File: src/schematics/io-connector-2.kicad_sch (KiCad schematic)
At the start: 1 part

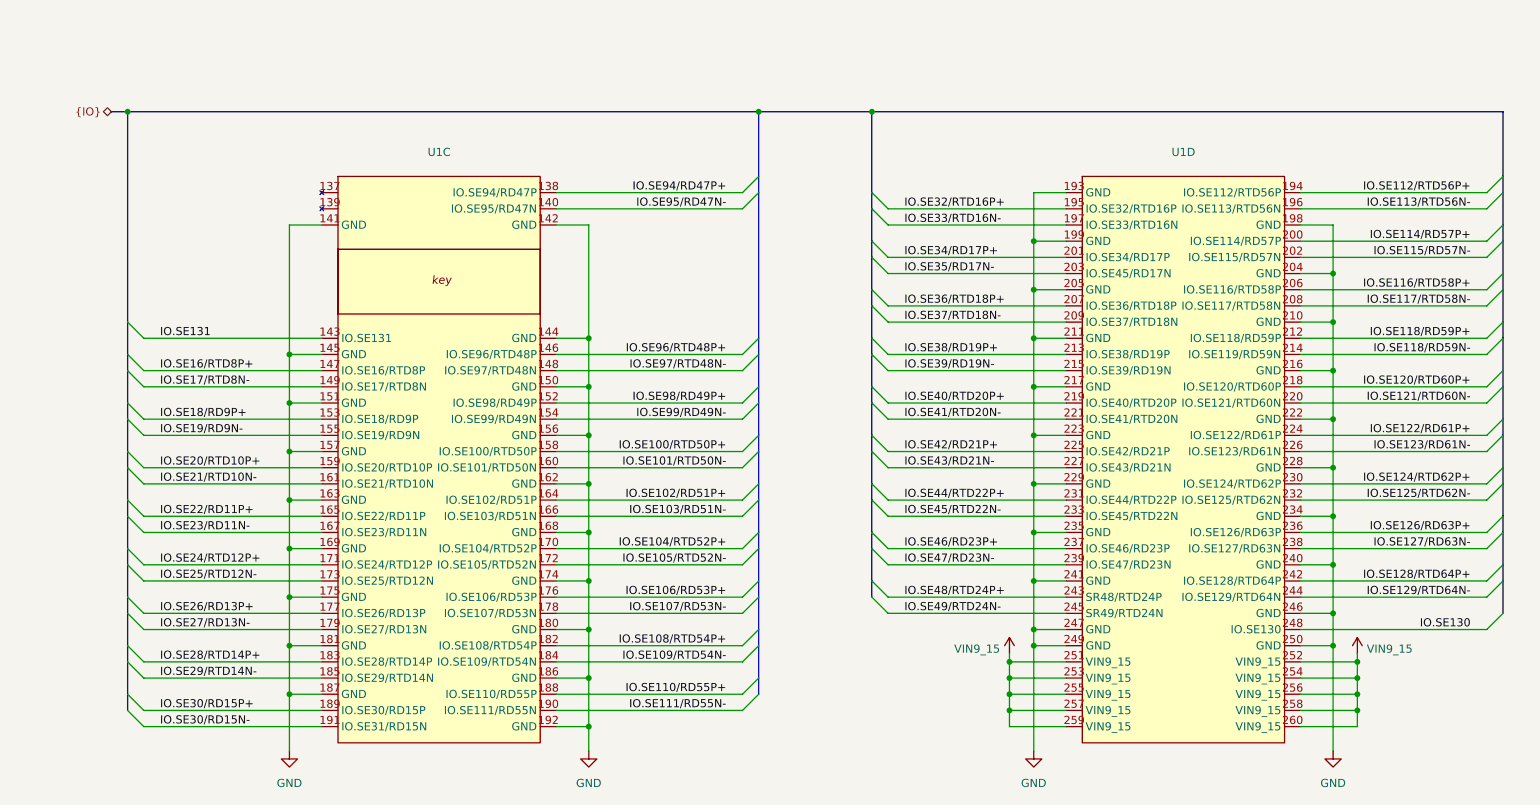
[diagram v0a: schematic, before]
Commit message: Adds draft of IO connector schematic connections to FPGA
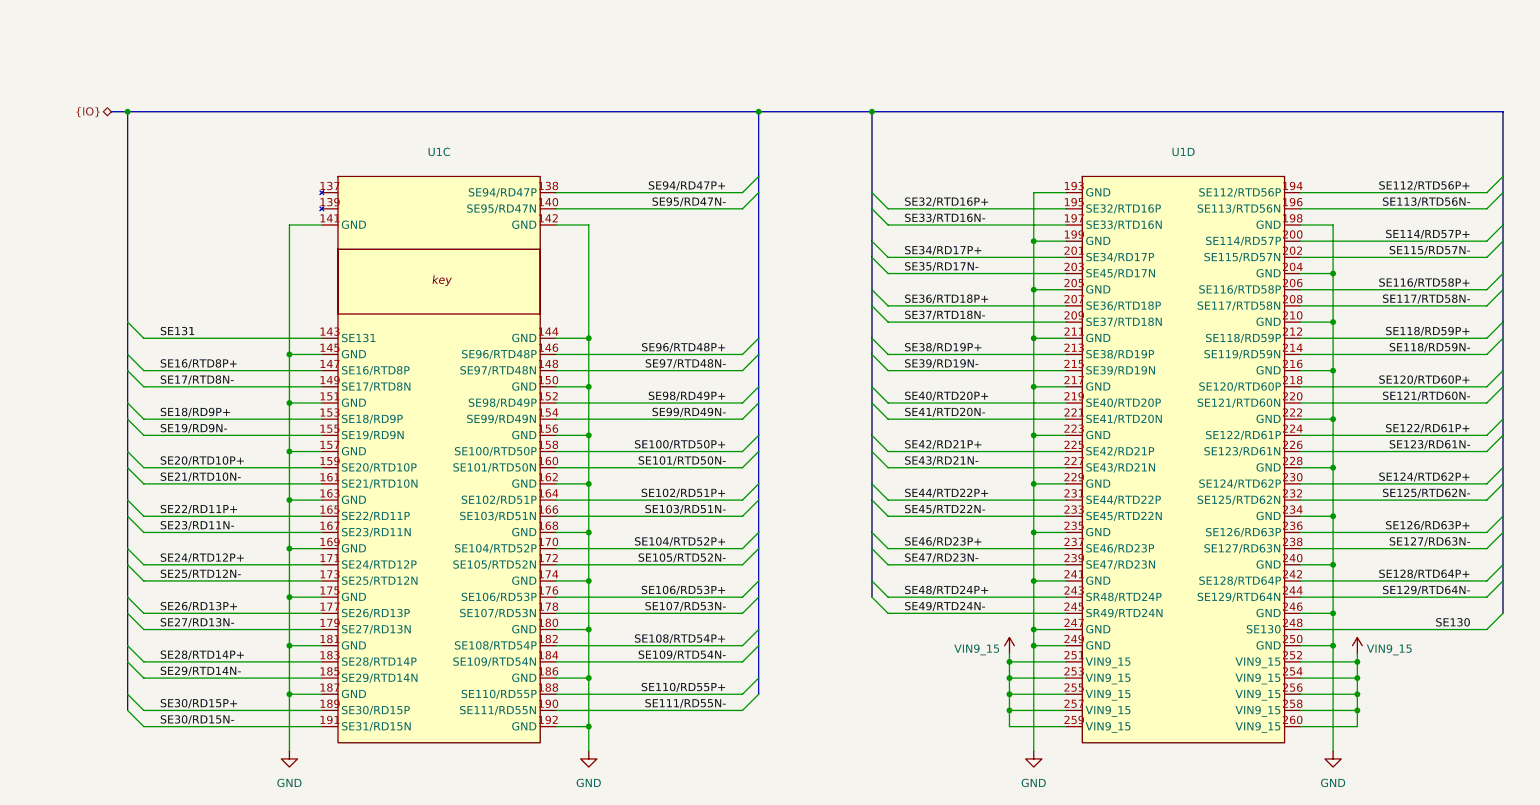
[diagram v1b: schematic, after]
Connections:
- net IO.SE100/RTD50P+ renamed SE100/RTD50P+
- net IO.SE101/RTD50N- renamed SE101/RTD50N-
- net IO.SE102/RD51P+ renamed SE102/RD51P+
- net IO.SE103/RD51N- renamed SE103/RD51N-
- net IO.SE104/RTD52P+ renamed SE104/RTD52P+
- net IO.SE105/RTD52N- renamed SE105/RTD52N-
- net IO.SE106/RD53P+ renamed SE106/RD53P+
- net IO.SE107/RD53N- renamed SE107/RD53N-
- net IO.SE108/RTD54P+ renamed SE108/RTD54P+
- net IO.SE109/RTD54N- renamed SE109/RTD54N-
- net IO.SE110/RD55P+ renamed SE110/RD55P+
- net IO.SE111/RD55N- renamed SE111/RD55N-
- net IO.SE112/RTD56P+ renamed SE112/RTD56P+
- net IO.SE113/RTD56N- renamed SE113/RTD56N-
- net IO.SE114/RD57P+ renamed SE114/RD57P+
- net IO.SE115/RD57N- renamed SE115/RD57N-
- net IO.SE116/RTD58P+ renamed SE116/RTD58P+
- net IO.SE117/RTD58N- renamed SE117/RTD58N-
- net IO.SE118/RD59N- renamed SE118/RD59N-
- net IO.SE118/RD59P+ renamed SE118/RD59P+
- net IO.SE120/RTD60P+ renamed SE120/RTD60P+
- net IO.SE121/RTD60N- renamed SE121/RTD60N-
- net IO.SE122/RD61P+ renamed SE122/RD61P+
- net IO.SE123/RD61N- renamed SE123/RD61N-
- net IO.SE124/RTD62P+ renamed SE124/RTD62P+
- net IO.SE125/RTD62N- renamed SE125/RTD62N-
- net IO.SE126/RD63P+ renamed SE126/RD63P+
- net IO.SE127/RD63N- renamed SE127/RD63N-
- net IO.SE128/RTD64P+ renamed SE128/RTD64P+
- net IO.SE129/RTD64N- renamed SE129/RTD64N-
- net IO.SE130 renamed SE130
- net IO.SE131 renamed SE131
- net IO.SE16/RTD8P+ renamed SE16/RTD8P+
- net IO.SE17/RTD8N- renamed SE17/RTD8N-
- net IO.SE18/RD9P+ renamed SE18/RD9P+
- net IO.SE19/RD9N- renamed SE19/RD9N-
- net IO.SE20/RTD10P+ renamed SE20/RTD10P+
- net IO.SE21/RTD10N- renamed SE21/RTD10N-
- net IO.SE22/RD11P+ renamed SE22/RD11P+
- net IO.SE23/RD11N- renamed SE23/RD11N-
- net IO.SE24/RTD12P+ renamed SE24/RTD12P+
- net IO.SE25/RTD12N- renamed SE25/RTD12N-
- net IO.SE26/RD13P+ renamed SE26/RD13P+
- net IO.SE27/RD13N- renamed SE27/RD13N-
- net IO.SE28/RTD14P+ renamed SE28/RTD14P+
- net IO.SE29/RTD14N- renamed SE29/RTD14N-
- net IO.SE30/RD15N- renamed SE30/RD15N-
- net IO.SE30/RD15P+ renamed SE30/RD15P+
- net IO.SE32/RTD16P+ renamed SE32/RTD16P+
- net IO.SE33/RTD16N- renamed SE33/RTD16N-
- net IO.SE34/RD17P+ renamed SE34/RD17P+
- net IO.SE35/RD17N- renamed SE35/RD17N-
- net IO.SE36/RTD18P+ renamed SE36/RTD18P+
- net IO.SE37/RTD18N- renamed SE37/RTD18N-
- net IO.SE38/RD19P+ renamed SE38/RD19P+
- net IO.SE39/RD19N- renamed SE39/RD19N-
- net IO.SE40/RTD20P+ renamed SE40/RTD20P+
- net IO.SE41/RTD20N- renamed SE41/RTD20N-
- net IO.SE42/RD21P+ renamed SE42/RD21P+
- net IO.SE43/RD21N- renamed SE43/RD21N-
- net IO.SE44/RTD22P+ renamed SE44/RTD22P+
- net IO.SE45/RTD22N- renamed SE45/RTD22N-
- net IO.SE46/RD23P+ renamed SE46/RD23P+
- net IO.SE47/RD23N- renamed SE47/RD23N-
- net IO.SE48/RTD24P+ renamed SE48/RTD24P+
- net IO.SE49/RTD24N- renamed SE49/RTD24N-
- net IO.SE94/RD47P+ renamed SE94/RD47P+
- net IO.SE95/RD47N- renamed SE95/RD47N-
- net IO.SE96/RTD48P+ renamed SE96/RTD48P+
- net IO.SE97/RTD48N- renamed SE97/RTD48N-
- net IO.SE98/RD49P+ renamed SE98/RD49P+
- net IO.SE99/RD49N- renamed SE99/RD49N-

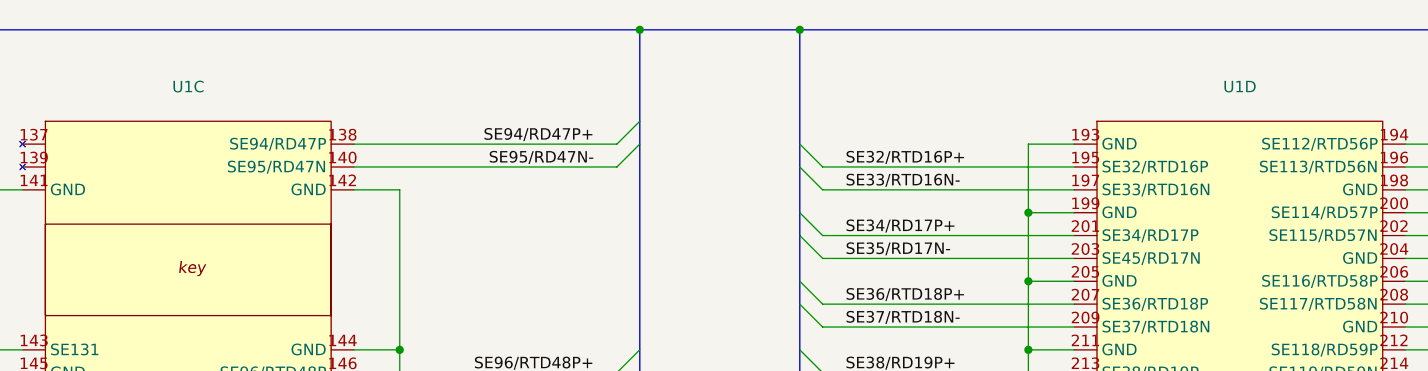
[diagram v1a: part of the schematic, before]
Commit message: Adds the clock oscillator
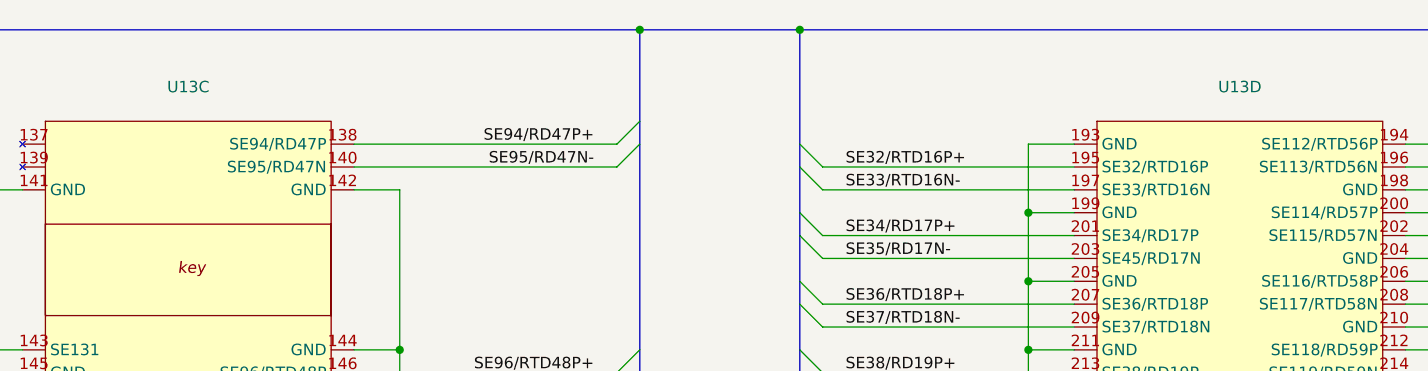
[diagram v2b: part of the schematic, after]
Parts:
- renumbered U1 to U13
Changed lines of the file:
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@@
 		(dnp no)
 		(fields_autoplaced yes)
-		(property "Reference" "U1"
+		(property "Reference" "U13"
 			(at 208.915 44.45 0)
 			(effects
@@
 			(project "ecap5-bsom"
 				(path "/c5fd18a3-9aa0-4151-b6e0-94da3d606686/25311f3d-42bc-4bc6-b069-9a914cc16127/b8034c88-bc29-48fe-94a3-92f685be2030"
-					(reference "U1")
+					(reference "U13")
 					(unit 4)
 				)
@@
 		(dnp no)
 		(fields_autoplaced yes)
-		(property "Reference" "#PWR033"
+		(property "Reference" "#PWR0149"
 			(at 115.57 144.78 0)
 			(effects
@@
 			(project "ecap5-bsom"
 				(path "/c5fd18a3-9aa0-4151-b6e0-94da3d606686/25311f3d-42bc-4bc6-b069-9a914cc16127/b8034c88-bc29-48fe-94a3-92f685be2030"
-					(reference "#PWR033")
+					(reference "#PWR0149")
 					(unit 1)
 				)
@@
 		(on_board yes)
 		(dnp no)
-		(property "Reference" "#PWR034"
+		(property "Reference" "#PWR0146"
 			(at 181.61 127 0)
 			(effects
@@
 			(project "ecap5-bsom"
 				(path "/c5fd18a3-9aa0-4151-b6e0-94da3d606686/25311f3d-42bc-4bc6-b069-9a914cc16127/b8034c88-bc29-48fe-94a3-92f685be2030"
-					(reference "#PWR034")
+					(reference "#PWR0146")
 					(unit 1)
 				)
@@
 	)
 	(symbol
-		(lib_name "IO_CONN_1")
 		(lib_id "ECAP5-BSOM:IO_CONN")
 		(at 92.71 92.71 0)
@@
 		(dnp no)
 		(fields_autoplaced yes)
-		(property "Reference" "U1"
+		(property "Reference" "U13"
 			(at 92.075 44.45 0)
 			(effects
@@
 			(project "ecap5-bsom"
 				(path "/c5fd18a3-9aa0-4151-b6e0-94da3d606686/25311f3d-42bc-4bc6-b069-9a914cc16127/b8034c88-bc29-48fe-94a3-92f685be2030"
-					(reference "U1")
+					(reference "U13")
 					(unit 3)
 				)
@@
 		(dnp no)
 		(fields_autoplaced yes)
-		(property "Reference" "#PWR036"
+		(property "Reference" "#PWR0151"
 			(at 232.41 144.78 0)
 			(effects
@@
 			(project "ecap5-bsom"
 				(path "/c5fd18a3-9aa0-4151-b6e0-94da3d606686/25311f3d-42bc-4bc6-b069-9a914cc16127/b8034c88-bc29-48fe-94a3-92f685be2030"
-					(reference "#PWR036")
+					(reference "#PWR0151")
 					(unit 1)
 				)
@@
 		(dnp no)
 		(fields_autoplaced yes)
-		(property "Reference" "#PWR030"
+		(property "Reference" "#PWR0148"
 			(at 68.58 144.78 0)
 			(effects
@@
 			(project "ecap5-bsom"
 				(path "/c5fd18a3-9aa0-4151-b6e0-94da3d606686/25311f3d-42bc-4bc6-b069-9a914cc16127/b8034c88-bc29-48fe-94a3-92f685be2030"
-					(reference "#PWR030")
+					(reference "#PWR0148")
 					(unit 1)
 				)
@@
 		(on_board yes)
 		(dnp no)
-		(property "Reference" "#PWR039"
+		(property "Reference" "#PWR0147"
 			(at 236.22 127 0)
 			(effects
@@
 			(project "ecap5-bsom"
 				(path "/c5fd18a3-9aa0-4151-b6e0-94da3d606686/25311f3d-42bc-4bc6-b069-9a914cc16127/b8034c88-bc29-48fe-94a3-92f685be2030"
-					(reference "#PWR039")
+					(reference "#PWR0147")
 					(unit 1)
 				)
@@
 		(dnp no)
 		(fields_autoplaced yes)
-		(property "Reference" "#PWR035"
+		(property "Reference" "#PWR0150"
 			(at 185.42 144.78 0)
 			(effects
@@
 			(project "ecap5-bsom"
 				(path "/c5fd18a3-9aa0-4151-b6e0-94da3d606686/25311f3d-42bc-4bc6-b069-9a914cc16127/b8034c88-bc29-48fe-94a3-92f685be2030"
-					(reference "#PWR035")
+					(reference "#PWR0150")
 					(unit 1)
 				)

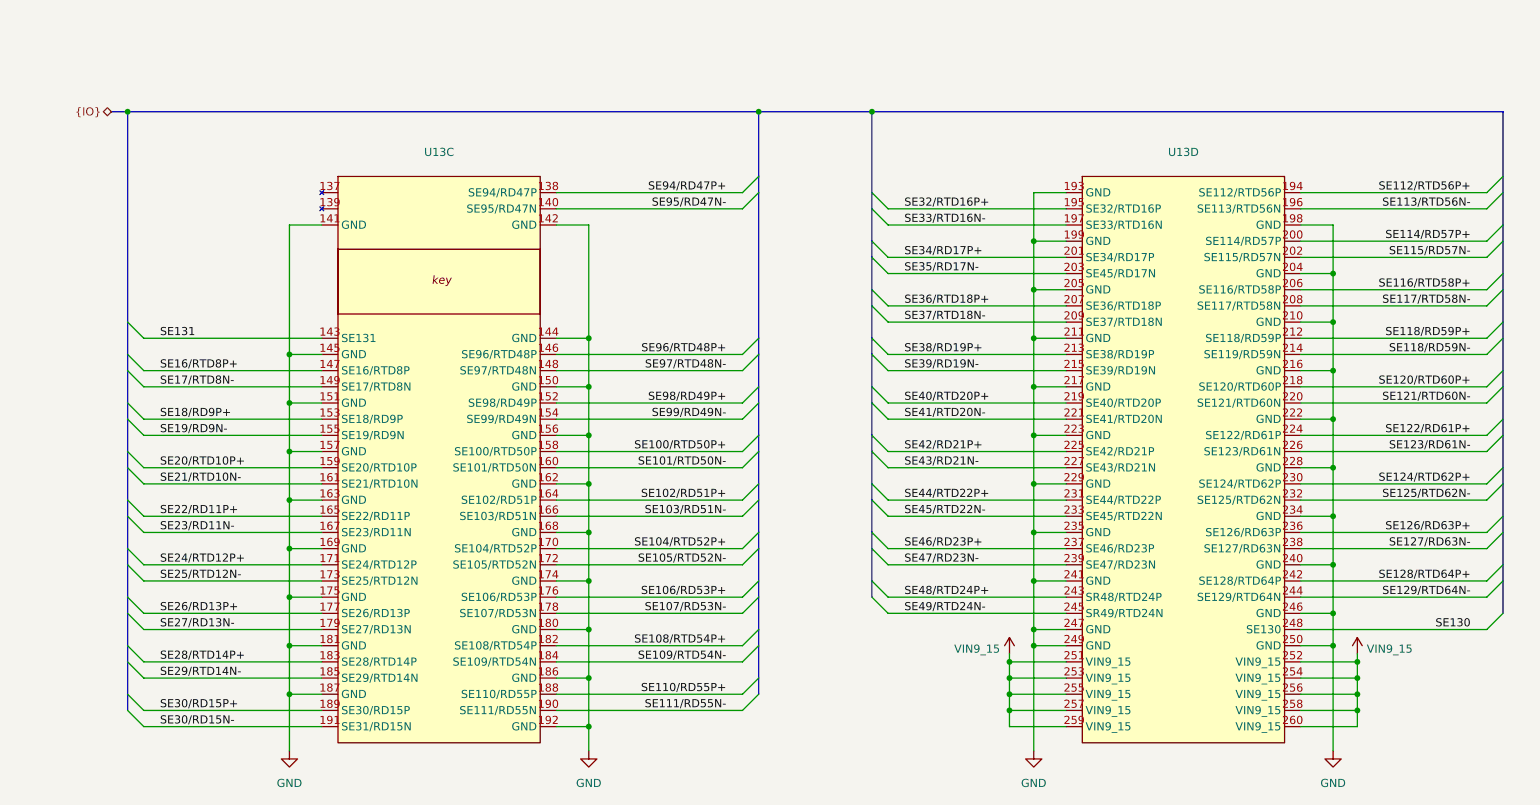
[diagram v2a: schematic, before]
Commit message: Adds bus aliases
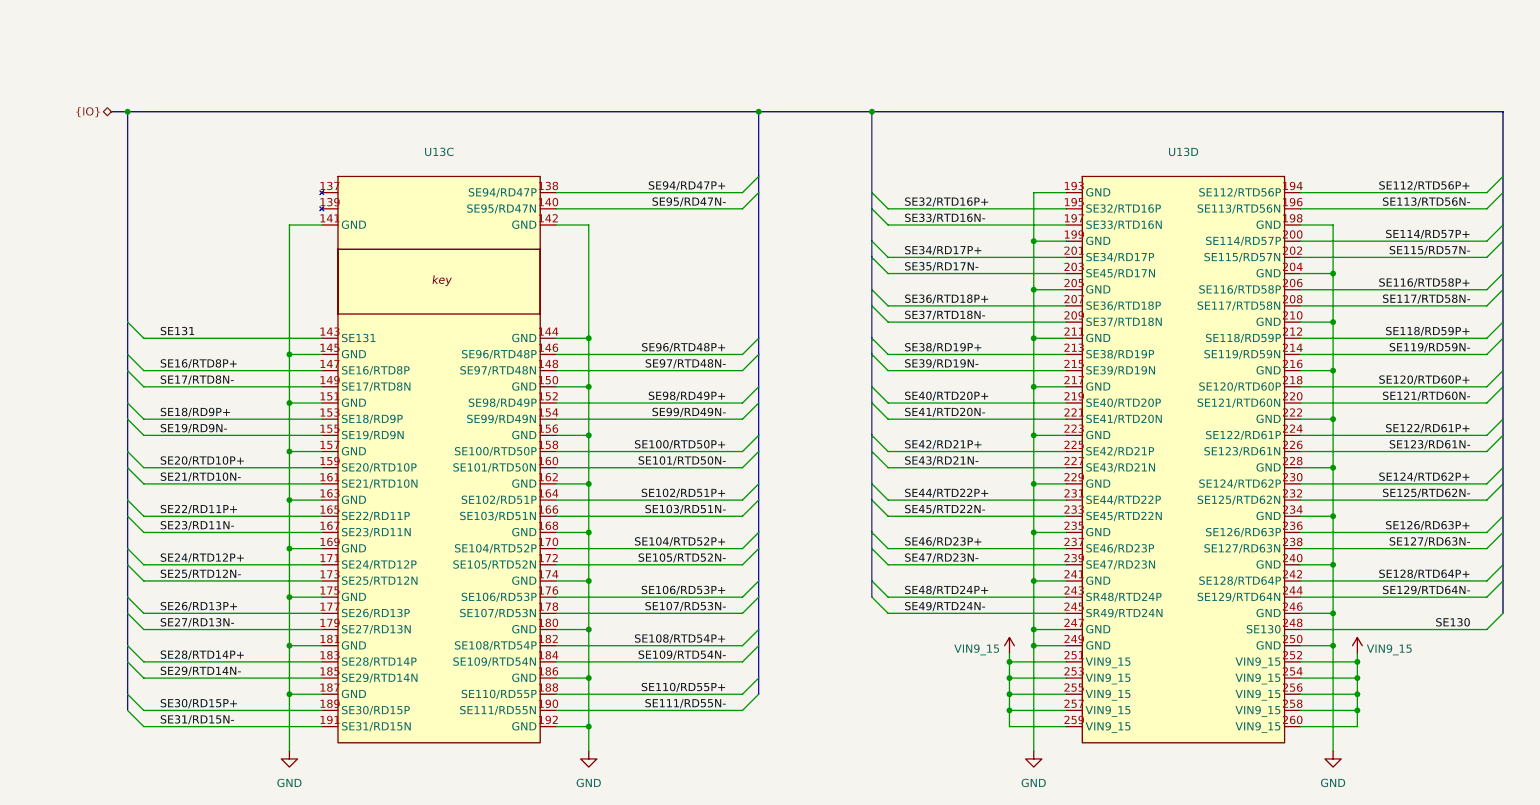
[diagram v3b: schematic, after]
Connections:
- net SE118/RD59N- renamed SE119/RD59N-
- net SE30/RD15N- renamed SE31/RD15N-
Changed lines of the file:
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@@
 		(rev "${Revision}")
 		(comment 1 "${Project Title}")
-		(comment 2 "IO CONNECTOR")
+		(comment 2 "IO CONNECTOR 2")
 		(comment 3 "${Part Number}")
 	)
@@
 		)
 	)
-	(label "SE30{slash}RD15N-"
+	(label "SE31{slash}RD15N-"
 		(at 48.26 134.62 0)
 		(fields_autoplaced yes)
@@
 		)
 	)
-	(label "SE118{slash}RD59N-"
+	(label "SE119{slash}RD59N-"
 		(at 254 76.2 180)
 		(fields_autoplaced yes)
